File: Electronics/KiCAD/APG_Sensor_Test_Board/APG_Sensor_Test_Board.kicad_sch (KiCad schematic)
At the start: 31 parts, among them J1 Conn_01x02, J2 Conn_01x06, J3 Conn_01x02

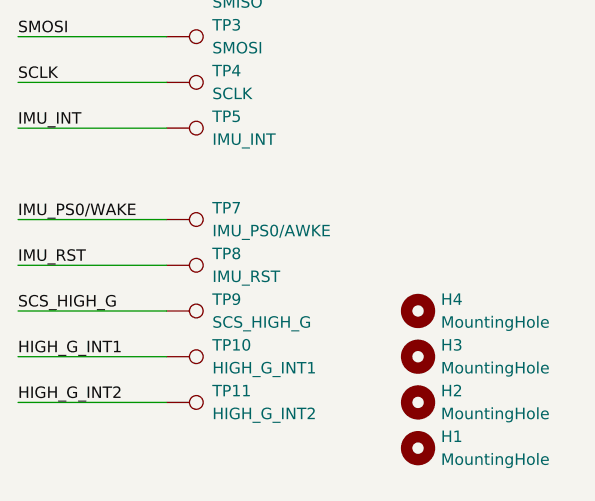
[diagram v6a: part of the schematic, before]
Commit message: Edit PCB and Update component values
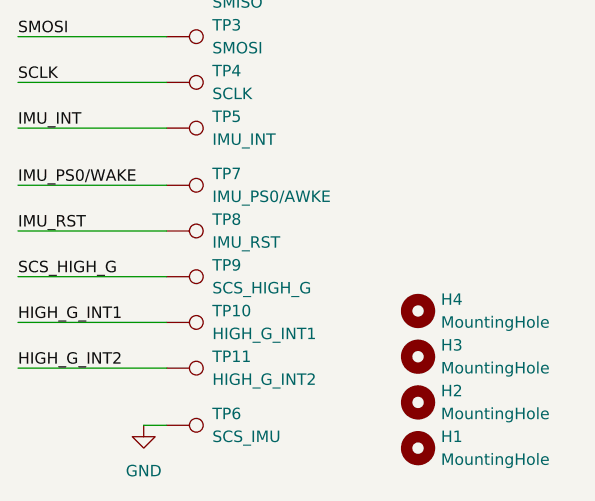
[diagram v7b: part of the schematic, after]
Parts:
- added TP6: SCS_IMU, TestPoint:TestPoint_Pad_D1.0mm, symbol Connector:TestPoint
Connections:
- net GND: now also TP6.1
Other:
- moved on the sheet: TP10, TP11, TP7, TP8, TP9
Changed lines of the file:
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@@
 	(wire
 		(pts
-			(xy 15.24 187.96) (xy 31.75 187.96)
+			(xy 15.24 184.15) (xy 31.75 184.15)
 		)
 		(stroke
@@
 	(wire
 		(pts
+			(xy 29.21 190.5) (xy 31.75 190.5)
+		)
+		(stroke
+			(width 0)
+			(type default)
+		)
+	)
+	(wire
+		(pts
 			(xy 157.48 40.64) (xy 184.15 40.64)
 		)
@@
 	(wire
 		(pts
-			(xy 15.24 177.8) (xy 31.75 177.8)
+			(xy 15.24 173.99) (xy 31.75 173.99)
 		)
 		(stroke
@@
 	(wire
 		(pts
-			(xy 15.24 167.64) (xy 31.75 167.64)
+			(xy 15.24 163.83) (xy 31.75 163.83)
 		)
 		(stroke
@@
 	(wire
 		(pts
-			(xy 15.24 172.72) (xy 31.75 172.72)
+			(xy 15.24 168.91) (xy 31.75 168.91)
 		)
 		(stroke
@@
 	(wire
 		(pts
-			(xy 15.24 182.88) (xy 31.75 182.88)
+			(xy 15.24 179.07) (xy 31.75 179.07)
 		)
 		(stroke
@@
 	)
 	(label "IMU_RST"
-		(at 15.24 172.72 0)
+		(at 15.24 168.91 0)
 		(fields_autoplaced yes)
 		(effects
@@
 	)
 	(label "IMU_PS0{slash}WAKE"
-		(at 15.24 167.64 0)
+		(at 15.24 163.83 0)
 		(fields_autoplaced yes)
 		(effects
@@
 	)
 	(label "SCS_HIGH_G"
-		(at 15.24 177.8 0)
+		(at 15.24 173.99 0)
 		(fields_autoplaced yes)
 		(effects
@@
 	)
 	(label "HIGH_G_INT1"
-		(at 15.24 182.88 0)
+		(at 15.24 179.07 0)
 		(fields_autoplaced yes)
 		(effects
@@
 	)
 	(label "HIGH_G_INT2"
-		(at 15.24 187.96 0)
+		(at 15.24 184.15 0)
 		(fields_autoplaced yes)
 		(effects
@@
 	(symbol
 		(lib_id "Connector:TestPoint")
-		(at 31.75 172.72 270)
+		(at 31.75 168.91 270)
 		(unit 1)
 		(exclude_from_sim no)
@@
 		(fields_autoplaced yes)
 		(property "Reference" "TP8"
-			(at 36.83 171.4499 90)
+			(at 36.83 167.6399 90)
 			(effects
 				(font
@@
 		)
 		(property "Value" "IMU_RST"
-			(at 36.83 173.9899 90)
+			(at 36.83 170.1799 90)
 			(effects
 				(font
@@
 		)
 		(property "Footprint" "TestPoint:TestPoint_Pad_D1.0mm"
-			(at 31.75 177.8 0)
+			(at 31.75 173.99 0)
 			(effects
 				(font
@@
 		)
 		(property "Datasheet" "~"
-			(at 31.75 177.8 0)
+			(at 31.75 173.99 0)
 			(effects
 				(font
@@
 		)
 		(property "Description" "test point"
-			(at 31.75 172.72 0)
+			(at 31.75 168.91 0)
 			(effects
 				(font
@@
 	)
 	(symbol
+		(lib_id "power:GND")
+		(at 29.21 190.5 0)
+		(unit 1)
+		(exclude_from_sim no)
+		(in_bom yes)
+		(on_board yes)
+		(dnp no)
+		(fields_autoplaced yes)
+		(property "Reference" "#PWR056"
+			(at 29.21 196.85 0)
+			(effects
+				(font
+					(size 1.27 1.27)
+				)
+				(hide yes)
+			)
+		)
+		(property "Value" "GND"
+			(at 29.21 195.58 0)
+			(effects
+				(font
+					(size 1.27 1.27)
+				)
+			)
+		)
+		(property "Footprint" ""
+			(at 29.21 190.5 0)
+			(effects
+				(font
+					(size 1.27 1.27)
+				)
+				(hide yes)
+			)
+		)
+		(property "Datasheet" ""
+			(at 29.21 190.5 0)
+			(effects
+				(font
+					(size 1.27 1.27)
+				)
+				(hide yes)
+			)
+		)
+		(property "Description" "Power symbol creates a global label with name \"GND\" , ground"
+			(at 29.21 190.5 0)
+			(effects
+				(font
+					(size 1.27 1.27)
+				)
+				(hide yes)
+			)
+		)
+		(pin "1"
+		)
+		(instances
+			(project "APG_Sensor_Test_Board"
+				(path "/3161be0c-372f-463d-be0a-bab00f344057"
+					(reference "#PWR056")
+					(unit 1)
+				)
+			)
+		)
+	)
+	(symbol
 		(lib_id "Mechanical:MountingHole")
 		(at 59.69 177.8 0)
@@
 	(symbol
 		(lib_id "Connector:TestPoint")
-		(at 31.75 187.96 270)
+		(at 31.75 184.15 270)
 		(unit 1)
 		(exclude_from_sim no)
@@
 		(fields_autoplaced yes)
 		(property "Reference" "TP11"
-			(at 36.83 186.6899 90)
+			(at 36.83 182.8799 90)
 			(effects
 				(font
@@
 		)
 		(property "Value" "HIGH_G_INT2"
-			(at 36.83 189.2299 90)
+			(at 36.83 185.4199 90)
 			(effects
 				(font
@@
 		)
 		(property "Footprint" "TestPoint:TestPoint_Pad_D1.0mm"
-			(at 31.75 193.04 0)
+			(at 31.75 189.23 0)
 			(effects
 				(font
@@
 		)
 		(property "Datasheet" "~"
-			(at 31.75 193.04 0)
+			(at 31.75 189.23 0)
 			(effects
 				(font
@@
 		)
 		(property "Description" "test point"
-			(at 31.75 187.96 0)
+			(at 31.75 184.15 0)
 			(effects
 				(font
@@
 	(symbol
 		(lib_id "Connector:TestPoint")
-		(at 31.75 177.8 270)
+		(at 31.75 173.99 270)
 		(unit 1)
 		(exclude_from_sim no)
@@
 		(fields_autoplaced yes)
 		(property "Reference" "TP9"
-			(at 36.83 176.5299 90)
+			(at 36.83 172.7199 90)
 			(effects
 				(font
@@
 		)
 		(property "Value" "SCS_HIGH_G"
-			(at 36.83 179.0699 90)
+			(at 36.83 175.2599 90)
 			(effects
 				(font
@@
 		)
 		(property "Footprint" "TestPoint:TestPoint_Pad_D1.0mm"
-			(at 31.75 182.88 0)
+			(at 31.75 179.07 0)
 			(effects
 				(font
@@
 		)
 		(property "Datasheet" "~"
-			(at 31.75 182.88 0)
+			(at 31.75 179.07 0)
 			(effects
 				(font
@@
 		)
 		(property "Description" "test point"
-			(at 31.75 177.8 0)
+			(at 31.75 173.99 0)
 			(effects
 				(font
@@
 	(symbol
 		(lib_id "Connector:TestPoint")
-		(at 31.75 167.64 270)
+		(at 31.75 163.83 270)
 		(unit 1)
 		(exclude_from_sim no)
@@
 		(fields_autoplaced yes)
 		(property "Reference" "TP7"
-			(at 36.83 166.3699 90)
+			(at 36.83 162.5599 90)
 			(effects
 				(font
@@
 		)
 		(property "Value" "IMU_PS0/AWKE"
-			(at 36.83 168.9099 90)
+			(at 36.83 165.0999 90)
 			(effects
 				(font
@@
 		)
 		(property "Footprint" "TestPoint:TestPoint_Pad_D1.0mm"
-			(at 31.75 172.72 0)
+			(at 31.75 168.91 0)
 			(effects
 				(font
@@
 		)
 		(property "Datasheet" "~"
-			(at 31.75 172.72 0)
+			(at 31.75 168.91 0)
 			(effects
 				(font
@@
 		)
 		(property "Description" "test point"
-			(at 31.75 167.64 0)
+			(at 31.75 163.83 0)
 			(effects
 				(font
@@
 	(symbol
 		(lib_id "Connector:TestPoint")
-		(at 31.75 182.88 270)
+		(at 31.75 179.07 270)
 		(unit 1)
 		(exclude_from_sim no)
@@
 		(fields_autoplaced yes)
 		(property "Reference" "TP10"
-			(at 36.83 181.6099 90)
+			(at 36.83 177.7999 90)
 			(effects
 				(font
@@
 		)
 		(property "Value" "HIGH_G_INT1"
-			(at 36.83 184.1499 90)
+			(at 36.83 180.3399 90)
 			(effects
 				(font
@@
 		)
 		(property "Footprint" "TestPoint:TestPoint_Pad_D1.0mm"
-			(at 31.75 187.96 0)
+			(at 31.75 184.15 0)
 			(effects
 				(font
@@
 		)
 		(property "Datasheet" "~"
-			(at 31.75 187.96 0)
+			(at 31.75 184.15 0)
 			(effects
 				(font
@@
 		)
 		(property "Description" "test point"
-			(at 31.75 182.88 0)
+			(at 31.75 179.07 0)
 			(effects
 				(font
@@
 					(unit 1)
 				)
+			)
+		)
+	)
+	(symbol
+		(lib_id "Connector:TestPoint")
+		(at 31.75 190.5 270)
+		(unit 1)
+		(exclude_from_sim no)
+		(in_bom yes)
+		(on_board yes)
+		(dnp no)
+		(fields_autoplaced yes)
+		(property "Reference" "TP6"
+			(at 36.83 189.2299 90)
+			(effects
+				(font
+					(size 1.27 1.27)
+				)
+				(justify left)
+			)
+		)
+		(property "Value" "SCS_IMU"
+			(at 36.83 191.7699 90)
+			(effects
+				(font
+					(size 1.27 1.27)
+				)
+				(justify left)
+			)
+		)
+		(property "Footprint" "TestPoint:TestPoint_Pad_D1.0mm"
+			(at 31.75 195.58 0)
+			(effects
+				(font
+					(size 1.27 1.27)
+				)
+				(hide yes)
+			)
+		)
+		(property "Datasheet" "~"
+			(at 31.75 195.58 0)
+			(effects
+				(font
+					(size 1.27 1.27)
+				)
+				(hide yes)
+			)
+		)
+		(property "Description" "test point"
+			(at 31.75 190.5 0)
+			(effects
+				(font
+					(size 1.27 1.27)
+				)
+				(hide yes)
+			)
+		)
+		(pin "1"
+		)
+		(instances
+			(project "APG_Sensor_Test_Board"
+				(path "/3161be0c-372f-463d-be0a-bab00f344057"
+					(reference "TP6")
+					(unit 1)
+				)

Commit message: APG Sensor Board V1.1 Production
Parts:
- TP6: value SCS_IMU -> GND
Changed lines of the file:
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@@
 			)
 		)
-		(property "Value" "SCS_IMU"
+		(property "Value" "GND"
 			(at 36.83 191.7699 90)
 			(effects
